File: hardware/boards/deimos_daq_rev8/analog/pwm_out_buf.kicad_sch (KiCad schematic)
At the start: 3 parts

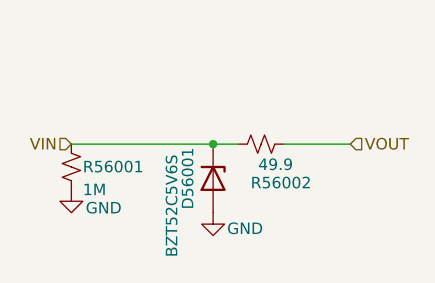
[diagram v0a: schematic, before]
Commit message: use better diode prot for digital I/O and dacs. generate fab files.
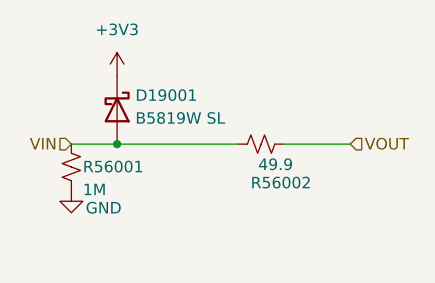
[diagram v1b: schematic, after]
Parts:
- removed D56001: BZT52C5V6S, Diode_SMD:D_SOD-323, symbol Device:D_Zener
- added D19001: B5819W SL, Diode_SMD:D_SOD-123, symbol Device:D_Schottky
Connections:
- net VIN: now also D19001.2 (A)
- new net +3V3: D19001.1 (K)
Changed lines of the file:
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@@
 	(paper "A4")
 	(junction
-		(at 143.764 92.456)
+		(at 133.096 92.456)
 		(diameter 0)
 		(color 0 0 0 0)
@@
 	(wire
 		(pts
-			(xy 128.016 92.456) (xy 143.764 92.456)
+			(xy 128.016 92.456) (xy 133.096 92.456)
 		)
 		(stroke
@@
 	(wire
 		(pts
-			(xy 143.764 92.456) (xy 146.558 92.456)
+			(xy 151.638 92.456) (xy 159.004 92.456)
 		)
 		(stroke
@@
 	(wire
 		(pts
-			(xy 151.638 92.456) (xy 159.004 92.456)
+			(xy 133.096 92.456) (xy 146.558 92.456)
 		)
 		(stroke
@@
 	)
 	(symbol
-		(lib_id "power:GND")
-		(at 143.764 100.076 0)
+		(lib_id "power:+3V3")
+		(at 133.096 84.836 0)
 		(unit 1)
 		(exclude_from_sim no)
@@
 		(on_board yes)
 		(dnp no)
-		(property "Reference" "#PWR282"
-			(at 143.764 106.426 0)
-			(effects
-				(font
-					(size 1.27 1.27)
-				)
-				(hide yes)
-			)
-		)
-		(property "Value" "GND"
-			(at 147.32 101.854 0)
+		(fields_autoplaced yes)
+		(property "Reference" "#PWR19002"
+			(at 133.096 88.646 0)
+			(effects
+				(font
+					(size 1.27 1.27)
+				)
+				(hide yes)
+			)
+		)
+		(property "Value" "+3V3"
+			(at 133.096 79.756 0)
 			(effects
 				(font
@@
 		)
 		(property "Footprint" ""
-			(at 143.764 100.076 0)
+			(at 133.096 84.836 0)
 			(effects
 				(font
@@
 		)
 		(property "Datasheet" ""
-			(at 143.764 100.076 0)
-			(effects
-				(font
-					(size 1.27 1.27)
-				)
-				(hide yes)
-			)
-		)
-		(property "Description" ""
-			(at 143.764 100.076 0)
+			(at 133.096 84.836 0)
+			(effects
+				(font
+					(size 1.27 1.27)
+				)
+				(hide yes)
+			)
+		)
+		(property "Description" "Power symbol creates a global label with name \"+3V3\""
+			(at 133.096 84.836 0)
 			(effects
 				(font
@@
 		)
 		(instances
-			(project "analog_i"
-				(path "/5a60c4b1-b6cb-416e-8883-8291fa089b87/c2baf18d-2b19-4edb-98b3-535275ee271f/2a5a8a5b-3176-4558-a595-780d8191c46b"
-					(reference "#PWR282")
-					(unit 1)
-				)
-				(path "/5a60c4b1-b6cb-416e-8883-8291fa089b87/c2baf18d-2b19-4edb-98b3-535275ee271f/3d57a2e8-76a3-4b72-b88d-c02ba9a3137f"
-					(reference "#PWR277")
-					(unit 1)
-				)
-				(path "/5a60c4b1-b6cb-416e-8883-8291fa089b87/c2baf18d-2b19-4edb-98b3-535275ee271f/489c5c16-982c-4958-8e55-03934daf9e33"
-					(reference "#PWR312")
-					(unit 1)
-				)
-				(path "/5a60c4b1-b6cb-416e-8883-8291fa089b87/c2baf18d-2b19-4edb-98b3-535275ee271f/ae776014-17b3-402b-a4e6-eaff991cef75"
-					(reference "#PWR307")
-					(unit 1)
-				)
-				(path "/5a60c4b1-b6cb-416e-8883-8291fa089b87/c2baf18d-2b19-4edb-98b3-535275ee271f/d157c6a6-e46c-46fa-8790-e34cb70ef5c4"
-					(reference "#PWR317")
-					(unit 1)
-				)
-				(path "/5a60c4b1-b6cb-416e-8883-8291fa089b87/c2baf18d-2b19-4edb-98b3-535275ee271f/d8ba479a-a7d9-47f0-902a-0be012b7ebf9"
-					(reference "#PWR302")
-					(unit 1)
-				)
-				(path "/5a60c4b1-b6cb-416e-8883-8291fa089b87/c2baf18d-2b19-4edb-98b3-535275ee271f/e5d59c3a-5602-4acb-ba66-19187ee13f4f"
-					(reference "#PWR367")
-					(unit 1)
-				)
-				(path "/5a60c4b1-b6cb-416e-8883-8291fa089b87/c2baf18d-2b19-4edb-98b3-535275ee271f/fbe215fd-185e-4781-8db8-c963f195ff3e"
-					(reference "#PWR287")
-					(unit 1)
-				)
-			)
 			(project "analog_frontend_panel"
 				(path "/c241d083-1323-4b4a-a540-956d0afb7b72/2a5a8a5b-3176-4558-a595-780d8191c46b"
-					(reference "#PWR19005")
+					(reference "#PWR19002")
 					(unit 1)
 				)
 				(path "/c241d083-1323-4b4a-a540-956d0afb7b72/3d57a2e8-76a3-4b72-b88d-c02ba9a3137f"
-					(reference "#PWR33009")
+					(reference "#PWR37001")
 					(unit 1)
 				)
@@
 				)
 				(path "/c241d083-1323-4b4a-a540-956d0afb7b72/d8ba479a-a7d9-47f0-902a-0be012b7ebf9"
-					(reference "#PWR27010")
+					(reference "#PWR27002")
 					(unit 1)
 				)
@@
 				)
 				(path "/c241d083-1323-4b4a-a540-956d0afb7b72/fbe215fd-185e-4781-8db8-c963f195ff3e"
-					(reference "#PWR26005")
+					(reference "#PWR26002")
 					(unit 1)
 				)
@@
 	)
 	(symbol
-		(lib_id "Device:D_Zener")
-		(at 143.764 96.266 270)
+		(lib_id "Device:D_Schottky")
+		(at 133.096 88.646 270)
 		(unit 1)
 		(exclude_from_sim no)
@@
 		(on_board yes)
 		(dnp no)
-		(property "Reference" "D56001"
-			(at 140.97 96.266 0)
-			(effects
-				(font
-					(size 1.27 1.27)
-				)
-			)
-		)
-		(property "Value" "BZT52C5V6S"
-			(at 139.192 99.314 0)
-			(effects
-				(font
-					(size 1.27 1.27)
-				)
-			)
-		)
-		(property "Footprint" "Diode_SMD:D_SOD-323"
-			(at 143.764 96.266 0)
+		(fields_autoplaced yes)
+		(property "Reference" "D19001"
+			(at 135.128 87.0584 90)
+			(effects
+				(font
+					(size 1.27 1.27)
+				)
+				(justify left)
+			)
+		)
+		(property "Value" "B5819W SL"
+			(at 135.128 89.5984 90)
+			(effects
+				(font
+					(size 1.27 1.27)
+				)
+				(justify left)
+			)
+		)
+		(property "Footprint" "Diode_SMD:D_SOD-123"
+			(at 133.096 88.646 0)
 			(effects
 				(font
@@
 		)
 		(property "Datasheet" "~"
-			(at 143.764 96.266 0)
-			(effects
-				(font
-					(size 1.27 1.27)
-				)
-				(hide yes)
-			)
-		)
-		(property "Description" ""
-			(at 143.764 96.266 0)
-			(effects
-				(font
-					(size 1.27 1.27)
-				)
-				(hide yes)
-			)
-		)
-		(property "LCSC" "C5184420"
-			(at 143.764 96.266 0)
-			(effects
-				(font
-					(size 1.27 1.27)
-				)
-				(hide yes)
-			)
+			(at 133.096 88.646 0)
+			(effects
+				(font
+					(size 1.27 1.27)
+				)
+				(hide yes)
+			)
+		)
+		(property "Description" "Schottky diode"
+			(at 133.096 88.646 0)
+			(effects
+				(font
+					(size 1.27 1.27)
+				)
+				(hide yes)
+			)
+		)
+		(property "LCSC" "C8598"
+			(at 133.096 88.646 0)
+			(effects
+				(font
+					(size 1.27 1.27)
+				)
+				(hide yes)
+			)
+		)
+		(pin "2"
 		)
 		(pin "1"
 		)
-		(pin "2"
-		)
 		(instances
-			(project "analog_i"
-				(path "/5a60c4b1-b6cb-416e-8883-8291fa089b87/c2baf18d-2b19-4edb-98b3-535275ee271f/2a5a8a5b-3176-4558-a595-780d8191c46b"
-					(reference "D56001")
-					(unit 1)
-				)
-				(path "/5a60c4b1-b6cb-416e-8883-8291fa089b87/c2baf18d-2b19-4edb-98b3-535275ee271f/3d57a2e8-76a3-4b72-b88d-c02ba9a3137f"
-					(reference "D55001")
-					(unit 1)
-				)
-				(path "/5a60c4b1-b6cb-416e-8883-8291fa089b87/c2baf18d-2b19-4edb-98b3-535275ee271f/489c5c16-982c-4958-8e55-03934daf9e33"
-					(reference "D60001")
-					(unit 1)
-				)
-				(path "/5a60c4b1-b6cb-416e-8883-8291fa089b87/c2baf18d-2b19-4edb-98b3-535275ee271f/ae776014-17b3-402b-a4e6-eaff991cef75"
-					(reference "D59001")
-					(unit 1)
-				)
-				(path "/5a60c4b1-b6cb-416e-8883-8291fa089b87/c2baf18d-2b19-4edb-98b3-535275ee271f/d157c6a6-e46c-46fa-8790-e34cb70ef5c4"
-					(reference "D61001")
-					(unit 1)
-				)
-				(path "/5a60c4b1-b6cb-416e-8883-8291fa089b87/c2baf18d-2b19-4edb-98b3-535275ee271f/d8ba479a-a7d9-47f0-902a-0be012b7ebf9"
-					(reference "D58001")
-					(unit 1)
-				)
-				(path "/5a60c4b1-b6cb-416e-8883-8291fa089b87/c2baf18d-2b19-4edb-98b3-535275ee271f/e5d59c3a-5602-4acb-ba66-19187ee13f4f"
-					(reference "D64001")
-					(unit 1)
-				)
-				(path "/5a60c4b1-b6cb-416e-8883-8291fa089b87/c2baf18d-2b19-4edb-98b3-535275ee271f/fbe215fd-185e-4781-8db8-c963f195ff3e"
-					(reference "D57001")
-					(unit 1)
-				)
-			)
 			(project "analog_frontend_panel"
 				(path "/c241d083-1323-4b4a-a540-956d0afb7b72/2a5a8a5b-3176-4558-a595-780d8191c46b"
@@
 				)
 				(path "/c241d083-1323-4b4a-a540-956d0afb7b72/3d57a2e8-76a3-4b72-b88d-c02ba9a3137f"
-					(reference "D33001")
-					(unit 1)
-				)
+					(reference "D37001")
+					(unit 1)
+				)
